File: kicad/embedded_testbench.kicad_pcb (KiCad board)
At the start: 2 copper layers, 121.2 x 56 mm, 127 parts, among them J1 12V INPUT, J10 VOUT4, J11 PM2, J12 SPI, J13 5V, J14 3V3, J15 GND, J16 UART, J17 OWI, J18 AIN2, J19 AIN3, J2 THMS1, J20 TWI1, J21 TWI2, J22 FDBK, J23 EXP, J24 WSN_NODE, J3 THMS2, J4 VOUT1, J5 UARTS, J6 CTRLS, J7 VOUT2, J8 VOUT3, J9 PM1, P1 RPi Header, Q1 BSS138, Q2 BSS138, Q3 BSS138, Q4 BSS138, Q5 BSS138, Q6 BSS138, U1 ADS1115IDGS, U10 INA219, U11 INA219, U12 INA219, U2 INA219, U3 INA219, U4 TCA9548APW, U5 MIC24045, U6 MIC24045, U7 MIC24045, U8 MIC24045, U9 INA219

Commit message: Updated schematic, PCB, and BOM (fixed part values and Farnell links)
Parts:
- R1, R2: value 10k -> 10k (0.1%)

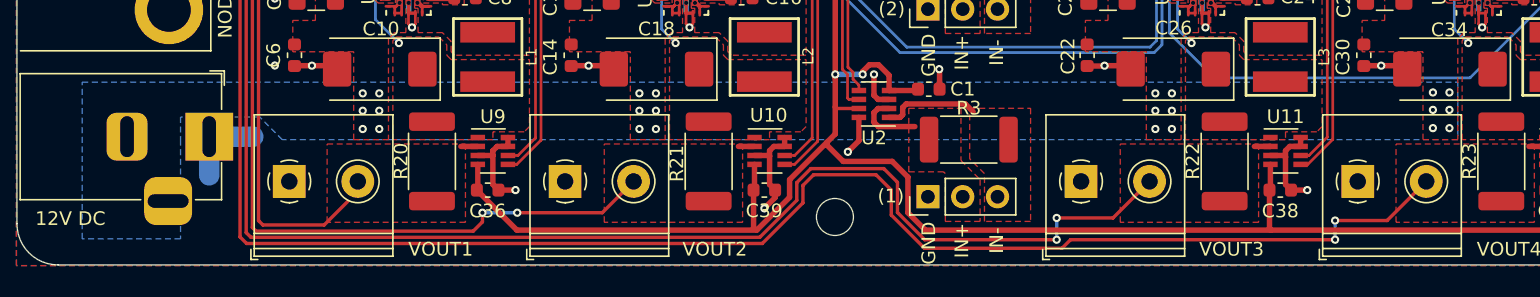
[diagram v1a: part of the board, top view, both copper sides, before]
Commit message: Fixed major PCB issue: wrongly connected 12V DC barrel jack
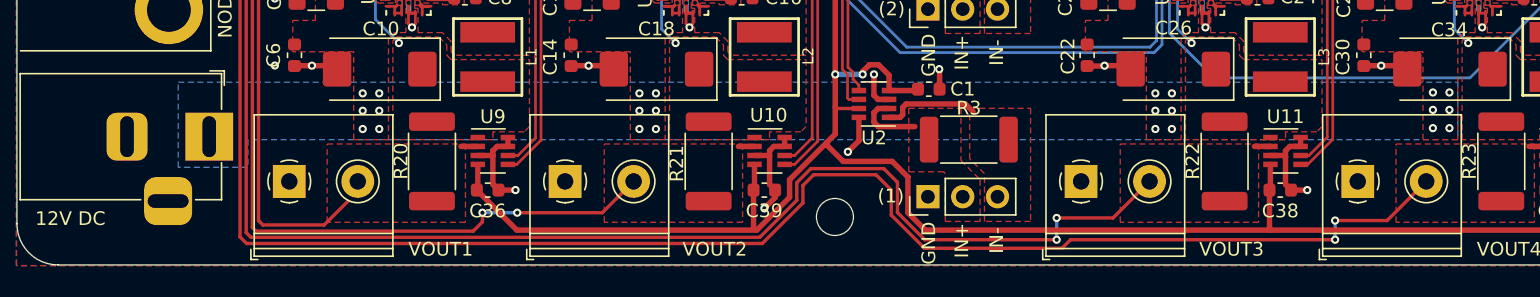
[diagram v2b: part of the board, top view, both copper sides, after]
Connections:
- J1 pad 1: GND -> +12V
- J1 pad 2: +12V -> GND
- J1 pad 3: +12V -> GND
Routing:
- net GND: track 232.0 -> 226.0 mm

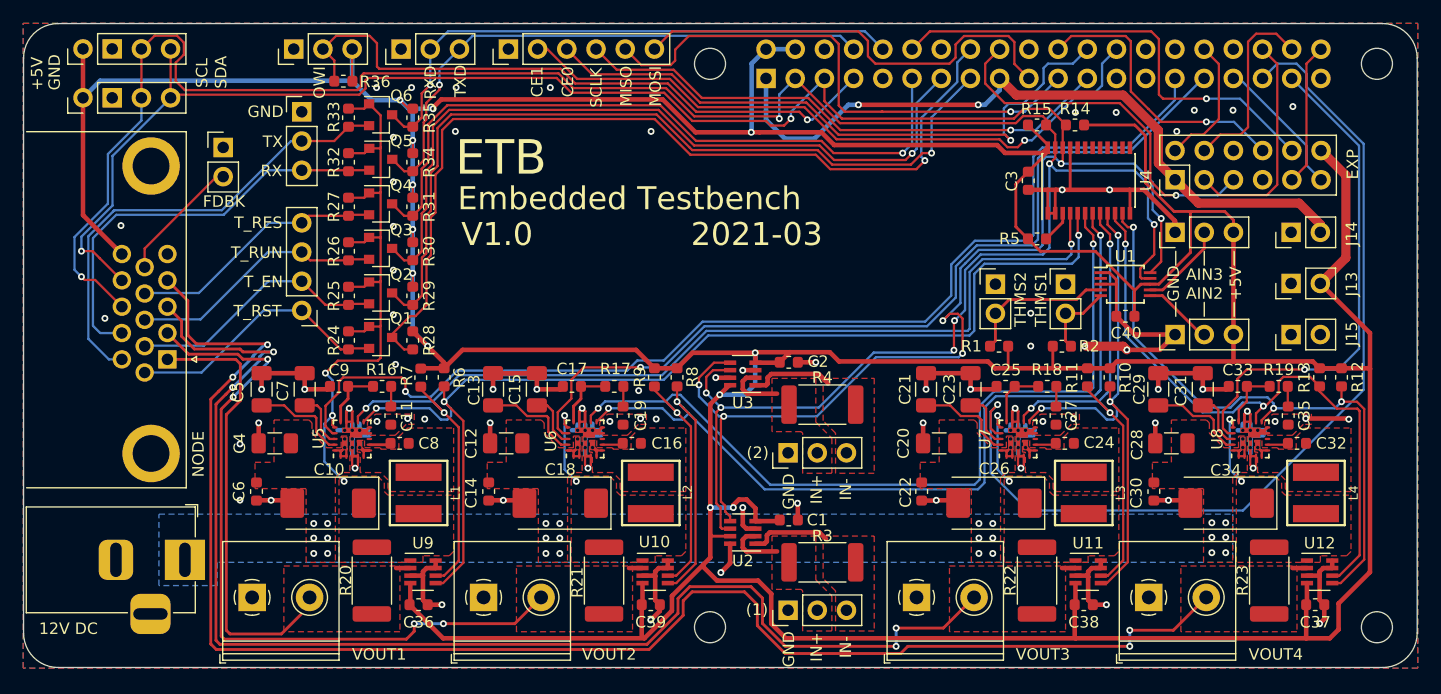
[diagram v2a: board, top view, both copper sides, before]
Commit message: Updated PCB design
Updated silk layer labels
Some minor improvements
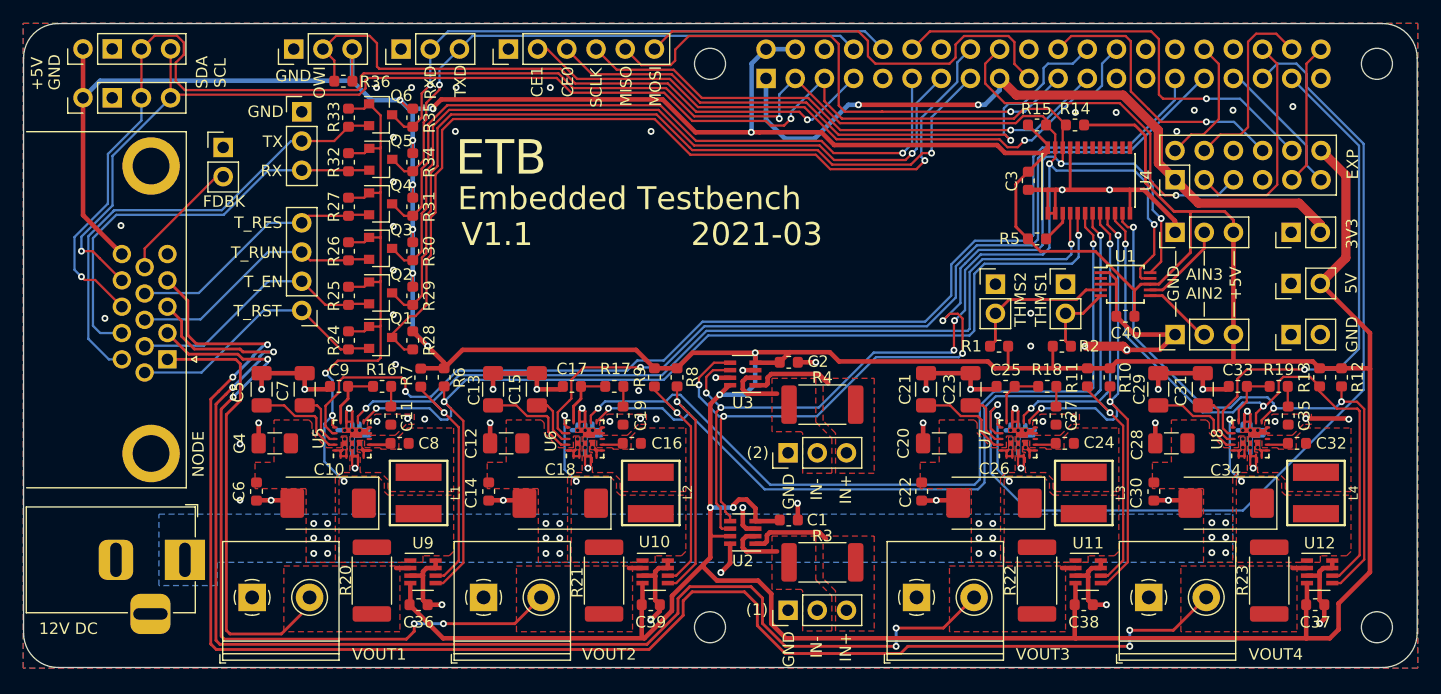
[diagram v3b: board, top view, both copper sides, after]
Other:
- board text added: "3V3"
- board text added: "5V"
- board text added: "V1.1"
- board text removed: "V1.0"
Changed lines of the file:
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@@
   (general
     (thickness 1.6)
-    (drawings 80)
+    (drawings 84)
     (tracks 1636)
     (zones 0)
@@
     (descr "Through hole straight pin header, 1x02, 2.54mm pitch, single row")
     (tags "Through hole pin header THT 1x02 2.54mm single row")
-    (fp_text reference J13 (at -0.0635 5.2705 90) (layer F.SilkS)
+    (fp_text reference J13 (at -0.0635 5.2705 90) (layer F.SilkS) hide
       (effects (font (size 1 1) (thickness 0.15)))
     )
@@
     (descr "Through hole straight pin header, 1x02, 2.54mm pitch, single row")
     (tags "Through hole pin header THT 1x02 2.54mm single row")
-    (fp_text reference J14 (at -0.127 5.2705 90) (layer F.SilkS)
+    (fp_text reference J14 (at -0.127 5.2705 90) (layer F.SilkS) hide
       (effects (font (size 1 1) (thickness 0.15)))
     )
@@
     (descr "Through hole straight pin header, 1x02, 2.54mm pitch, single row")
     (tags "Through hole pin header THT 1x02 2.54mm single row")
-    (fp_text reference J15 (at 0.0635 5.2705 90) (layer F.SilkS)
+    (fp_text reference J15 (at 0.0635 5.2705 90) (layer F.SilkS) hide
       (effects (font (size 1 1) (thickness 0.15)))
     )
@@
     )
   )
+  (gr_text GND (at 91.059 73.152) (layer F.SilkS)
+    (effects (font (size 1 1) (thickness 0.15)))
+  )
+  (gr_text 5V (at 183.0705 91.186 90) (layer F.SilkS)
+    (effects (font (size 1 1) (thickness 0.15)))
+  )
+  (gr_text 3V3 (at 183.134 86.868 90) (layer F.SilkS)
+    (effects (font (size 1 1) (thickness 0.15)))
+  )
+  (gr_text GND (at 183.134 95.631 90) (layer F.SilkS)
+    (effects (font (size 1 1) (thickness 0.15)))
+  )
   (gr_text GND (at 70.2945 72.8345 90) (layer F.SilkS)
     (effects (font (size 1 1) (thickness 0.15)))
@@
     (effects (font (size 1 1) (thickness 0.15)))
   )
-  (gr_text SCL (at 83.1215 72.898 90) (layer F.SilkS)
+  (gr_text SCL (at 84.709 72.898 90) (layer F.SilkS)
     (effects (font (size 1 1) (thickness 0.15)))
   )
@@
     (effects (font (size 2 2) (thickness 0.3)) (justify right))
   )
-  (gr_text V1.0 (at 105.664 86.9315) (layer F.SilkS)
+  (gr_text V1.1 (at 105.664 86.9315) (layer F.SilkS)
     (effects (font (size 2 2) (thickness 0.3)) (justify left))
   )
@@
     (effects (font (size 1 1) (thickness 0.15)))
   )
-  (gr_text SDA (at 84.7725 72.8345 90) (layer F.SilkS)
+  (gr_text SDA (at 83.1215 72.8345 90) (layer F.SilkS)
     (effects (font (size 1 1) (thickness 0.15)))
   )
@@
     (effects (font (size 1 1) (thickness 0.15)))
   )
-  (gr_text IN- (at 139.1035 109.106 90) (layer F.SilkS)
+  (gr_text IN+ (at 139.1035 109.106 90) (layer F.SilkS)
     (effects (font (size 1 1) (thickness 0.15)))
   )
-  (gr_text IN+ (at 136.5635 109.106 90) (layer F.SilkS)
+  (gr_text IN- (at 136.5635 109.106 90) (layer F.SilkS)
     (effects (font (size 1 1) (thickness 0.15)))
   )
@@
     (effects (font (size 1 1) (thickness 0.15)))
   )
-  (gr_text IN- (at 139.1035 122.822 90) (layer F.SilkS)
+  (gr_text IN+ (at 139.1035 122.822 90) (layer F.SilkS)
     (effects (font (size 1 1) (thickness 0.15)))
   )
-  (gr_text IN+ (at 136.5635 122.822 90) (layer F.SilkS)
+  (gr_text IN- (at 136.5635 122.822 90) (layer F.SilkS)
     (effects (font (size 1 1) (thickness 0.15)))
   )

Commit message: More fixes to PCB silk layer
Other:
- board text added: "THMS0"
- board text removed: "THMS2"
